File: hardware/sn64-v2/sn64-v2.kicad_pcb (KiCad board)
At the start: 6 copper layers, 111 x 80.5 mm, 182 parts, among them J1 N64 cartridge edge, J101 DX07S016JA3R1500, J2 SNES cartridge socket 62, U1 LFE5U-85F-8BG381I, U10 TLV62569DBVR, U11 AP2112K-2.5TRG1, U12 TPS2553DBVR, U2 W25Q128JVSIQ, U201 SN74ALVC164245DGGR, U202 SN74ALVC164245DGGR, U203 SN74ALVC164245DGGR, U204 SN74ALVC164245DGGR, U205 SN74LVC07APWR, U3 TPS3808G01DBVR, U4 USBLC6-2SC6, U6 TLA2528IRTER, U7 TPS2121RUXR, U8 TPS63070RNMR, U9 TLV62569DBVR, X1 27MHz 1631-27005-BTBEYA

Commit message: Licences, attribution notice and credits; credit line on the v2 board silkscreen
- GPL-3.0-or-later for the code, CERN-OHL-S-2.0 for the hardware and docs (texts at the
  top level, LICENSING.md explains what applies to what).
- NOTICE: "SN64 by FantomZap" with the repository as source location, as a GPL-3.0
  section 7(b) term for the code and a CERN-OHL-S notice for the hardware.
- CREDITS.md: the projects and people SN64 borrows from, what was used, and under
  which licence.
- v2 board: the credit and source location on the front silkscreen; DRC unchanged.

Co-Authored-By: Claude Opus 5.5 <noreply@anthropic.com>
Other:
- board text added: "SN64 by FantomZap github.com/FantomZap/SN-64 CERN-OHL-S-2.0"
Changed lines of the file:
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@@
 		(layer "Edge.Cuts")
+	)
+	(gr_text "SN64 by FantomZap   github.com/FantomZap/SN-64   CERN-OHL-S-2.0"
+		(at 0 -61 0)
+		(layer "F.SilkS")
+		(effects
+			(font
+				(size 1 1)
+				(thickness 0.15)
+			)
+		)
 	)
 	(segment

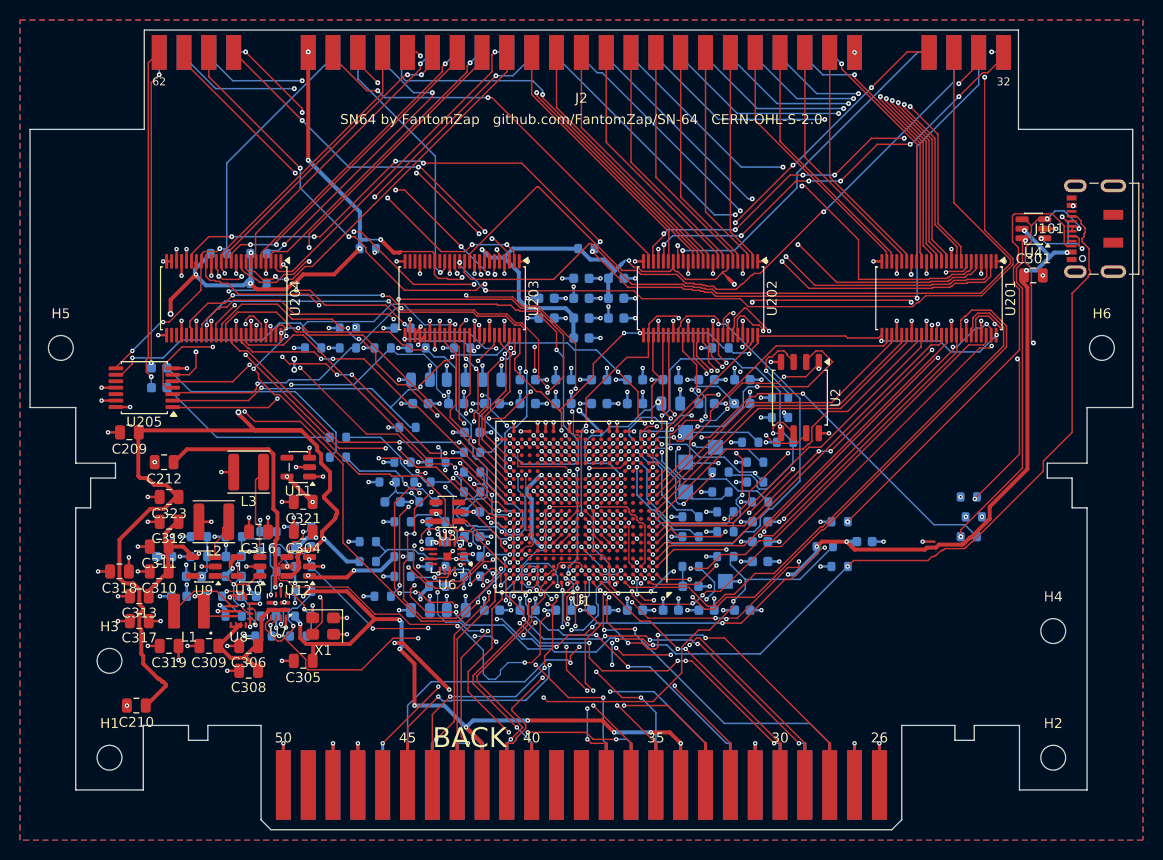
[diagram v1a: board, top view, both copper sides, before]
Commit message: v2 board refitted to the shorter shell: top edge 60 mm, USB-C at 32.5 mm
The owner approved the 10 mm shorter shell, so the routed board was refitted to it with
refit_tower_v2.py (new geometry short-60, applied to the tower-70 board):

- Outline 111 mm wide from 26.4 to 50 mm, 88 mm neck to the top edge at 60; socket pads
  10 mm lower. USB-C and its ESD part at 32.5 mm, VBUS capacitor above them, mounting
  holes H5/H6 at 44.5, silkscreen credit line at 50.5.
- 64 nets routed again (59 socket nets, 5 USB nets) with all other copper locked. The
  default ordering left the cartridge master clock boxed in; the router's bus ordering
  routed all 64 on the same three layers.
- 3,603 tracks, 1,066 vias, 213 of 218 signal nets fully connected, the same 6 open items;
  DRC errors: 6 single-spoke thermal reliefs (5 before).
- Board renders, copper picture, STEP and check reports regenerated. The board STEP with
  all part models has no interference with the shorter shell, the cartridge or its PCB.
- Shell model: board-60 is the default geometry and matches the board; board-70 stays for
  comparison. compare-70-vs-60.png shows before and after.

Schematic, FPGA pin plan and build_v2_pcb.py are unchanged.

Co-Authored-By: Claude Opus 5.5 <noreply@anthropic.com>
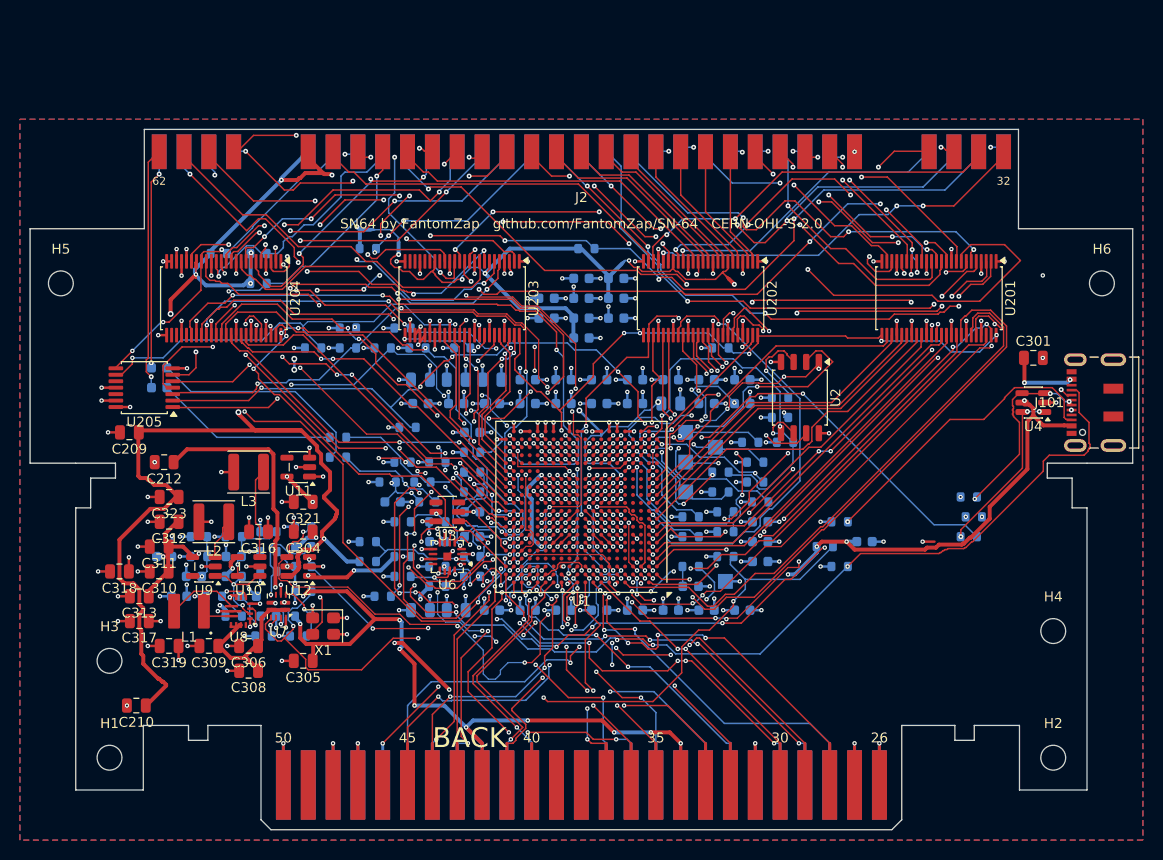
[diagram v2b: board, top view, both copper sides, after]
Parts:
- moved J101 17.5 mm to (52.4, -32.5)
- moved U4 17.5 mm to (45.5, -32.5)
- moved J2 10.0 mm to (0.00, -60.0)
- moved C301 8.30 mm to (45.5, -37.0)
- moved H5 6.50 mm to (-52.4, -44.5)
- moved H6 6.50 mm to (52.4, -44.5)
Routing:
- net SNES_PA7: track 84.9 -> 57.0 mm, vias 0 -> 5
- net SNES_SYSTEM_CLK: track 83.2 -> 60.3 mm
- net USB_DN: track 45.3 -> 22.9 mm
- net USB_DP: track 40.6 -> 20.2 mm, vias 6 -> 4
- net SNES_EXPAND: track 111.9 -> 93.8 mm, vias 7 -> 8
- net USB_CC2: track 115.4 -> 99.4 mm
- net USB_CC1: track 121.4 -> 105.4 mm
- net SNES_CIC_DATA1: track 51.3 -> 37.5 mm, vias 5 -> 2
- net USB_VBUS: track 136.3 -> 123.9 mm, vias 11 -> 10
- net SNES_A20: track 24.2 -> 13.1 mm
- net SNES_PA6: track 68.0 -> 57.2 mm, vias 1 -> 5
- net SNES_A6: track 39.1 -> 28.4 mm, vias 2 -> 4
- net SNES_A8: track 33.0 -> 23.0 mm, vias 2 -> 4
- net SNES_AUDIO_R_IN: track 34.5 -> 24.5 mm
- net SNES_AUDIO_L_IN: track 32.1 -> 22.1 mm
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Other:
- board size 111 x 80.5 mm -> 111 x 70.5 mm
